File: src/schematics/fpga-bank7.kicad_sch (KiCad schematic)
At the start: 7 parts, among them U6 LFE5U-85F-*BG756*

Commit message: Add remaining component footprints (#79)
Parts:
- C78, C79, C80, C81, C82, C83: footprint (none) -> Capacitor_SMD:C_0402_1005Metric
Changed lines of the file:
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@@
 			)
 		)
-		(property "Footprint" ""
+		(property "Footprint" "Capacitor_SMD:C_0402_1005Metric"
 			(at 165.1 36.83 0)
 			(effects
@@
 			)
 		)
-		(property "Footprint" ""
+		(property "Footprint" "Capacitor_SMD:C_0402_1005Metric"
 			(at 153.67 36.83 0)
 			(effects
@@
 			)
 		)
-		(property "Footprint" ""
+		(property "Footprint" "Capacitor_SMD:C_0402_1005Metric"
 			(at 123.19 36.83 0)
 			(effects
@@
 			)
 		)
-		(property "Footprint" ""
+		(property "Footprint" "Capacitor_SMD:C_0402_1005Metric"
 			(at 133.35 36.83 0)
 			(effects
@@
 			)
 		)
-		(property "Footprint" ""
+		(property "Footprint" "Capacitor_SMD:C_0402_1005Metric"
 			(at 113.03 36.83 0)
 			(effects
@@
 			)
 		)
-		(property "Footprint" ""
+		(property "Footprint" "Capacitor_SMD:C_0402_1005Metric"
 			(at 143.51 36.83 0)
 			(effects

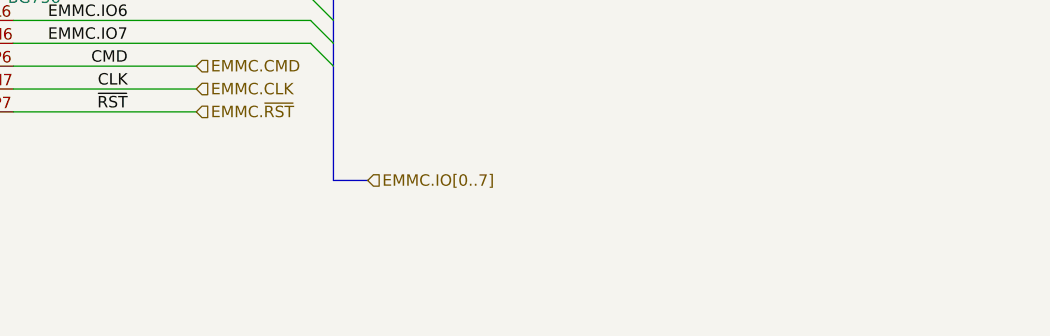
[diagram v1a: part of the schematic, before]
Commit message: Add notes on the schematic
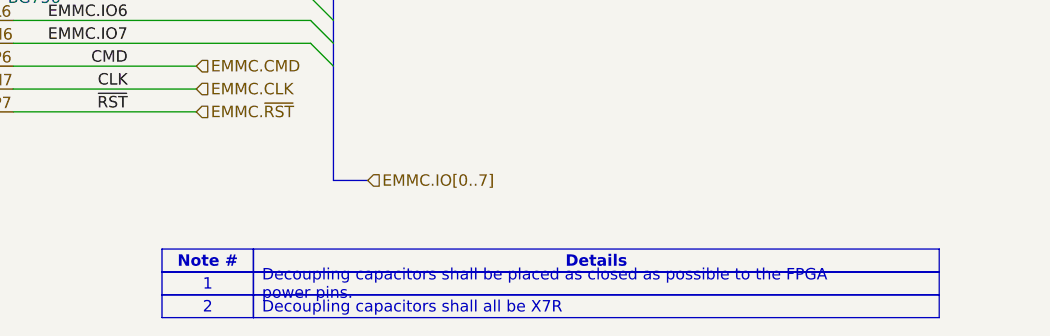
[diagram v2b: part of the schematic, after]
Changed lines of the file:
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@@
 		(comment 3 "${Part Number}")
+	)
+	(text_box "Decoupling capacitors shall all be X7R"
+		(exclude_from_sim no)
+		(at 203.2 167.64 0)
+		(size 76.2 2.54)
+		(margins 0.9525 0.9525 0.9525 0.9525)
+		(stroke
+			(width 0)
+			(type solid)
+			(color 0 0 0 1)
+		)
+		(fill
+			(type none)
+		)
+		(effects
+			(font
+				(face "Arial")
+				(size 1.27 1.27)
+				(color 0 0 0 1)
+			)
+			(justify left)
+		)
+	)
+	(text_box "Decoupling capacitors shall be placed as closed as possible to the FPGA power pins."
+		(exclude_from_sim no)
+		(at 203.2 165.1 0)
+		(size 76.2 2.54)
+		(margins 0.9525 0.9525 0.9525 0.9525)
+		(stroke
+			(width 0)
+			(type solid)
+			(color 0 0 0 1)
+		)
+		(fill
+			(type none)
+		)
+		(effects
+			(font
+				(face "Arial")
+				(size 1.27 1.27)
+				(color 0 0 0 1)
+			)
+			(justify left)
+		)
+	)
+	(text_box "2"
+		(exclude_from_sim no)
+		(at 193.04 167.64 0)
+		(size 10.16 2.54)
+		(margins 0.9525 0.9525 0.9525 0.9525)
+		(stroke
+			(width 0)
+			(type solid)
+			(color 0 0 0 1)
+		)
+		(fill
+			(type none)
+		)
+		(effects
+			(font
+				(face "Arial")
+				(size 1.27 1.27)
+				(color 0 0 0 1)
+			)
+		)
+	)
+	(text_box "Details"
+		(exclude_from_sim no)
+		(at 203.2 162.56 0)
+		(size 76.2 2.54)
+		(margins 0.9525 0.9525 0.9525 0.9525)
+		(stroke
+			(width 0)
+			(type solid)
+			(color 0 0 0 1)
+		)
+		(fill
+			(type none)
+		)
+		(effects
+			(font
+				(face "Arial")
+				(size 1.27 1.27)
+				(bold yes)
+				(color 0 0 0 1)
+			)
+		)
+	)
+	(text_box "Note #"
+		(exclude_from_sim no)
+		(at 193.04 162.56 0)
+		(size 10.16 2.54)
+		(margins 0.9525 0.9525 0.9525 0.9525)
+		(stroke
+			(width 0)
+			(type solid)
+			(color 0 0 0 1)
+		)
+		(fill
+			(type none)
+		)
+		(effects
+			(font
+				(face "Arial")
+				(size 1.27 1.27)
+				(bold yes)
+				(color 0 0 0 1)
+			)
+		)
+	)
+	(text_box "1"
+		(exclude_from_sim no)
+		(at 193.04 165.1 0)
+		(size 10.16 2.54)
+		(margins 0.9525 0.9525 0.9525 0.9525)
+		(stroke
+			(width 0)
+			(type solid)
+			(color 0 0 0 1)
+		)
+		(fill
+			(type none)
+		)
+		(effects
+			(font
+				(face "Arial")
+				(size 1.27 1.27)
+				(color 0 0 0 1)
+			)
+		)
 	)
 	(junction

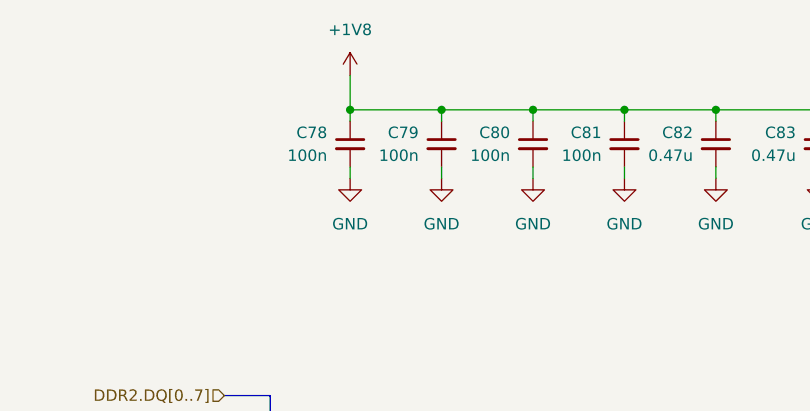
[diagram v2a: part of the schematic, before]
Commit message: Adds decoupling capacitors
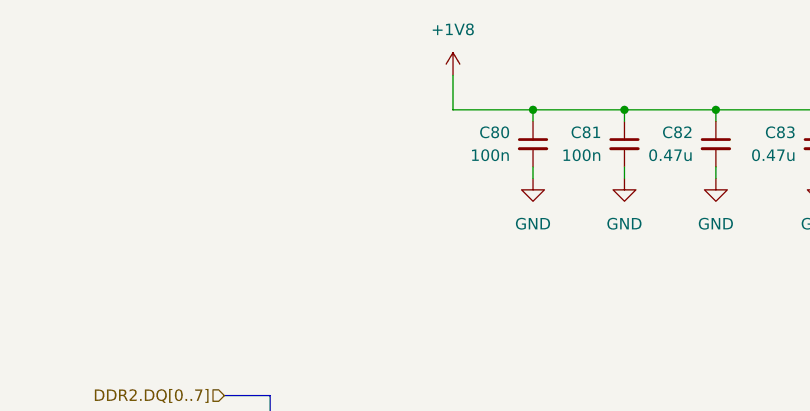
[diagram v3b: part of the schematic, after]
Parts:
- removed C78, C79: 100n, Capacitor_SMD:C_0402_1005Metric, symbol Device:C_Small
- C80, C81, C82, C83: footprint Capacitor_SMD:C_0402_1005Metric -> Capacitor_SMD:C_0201_0603Metric

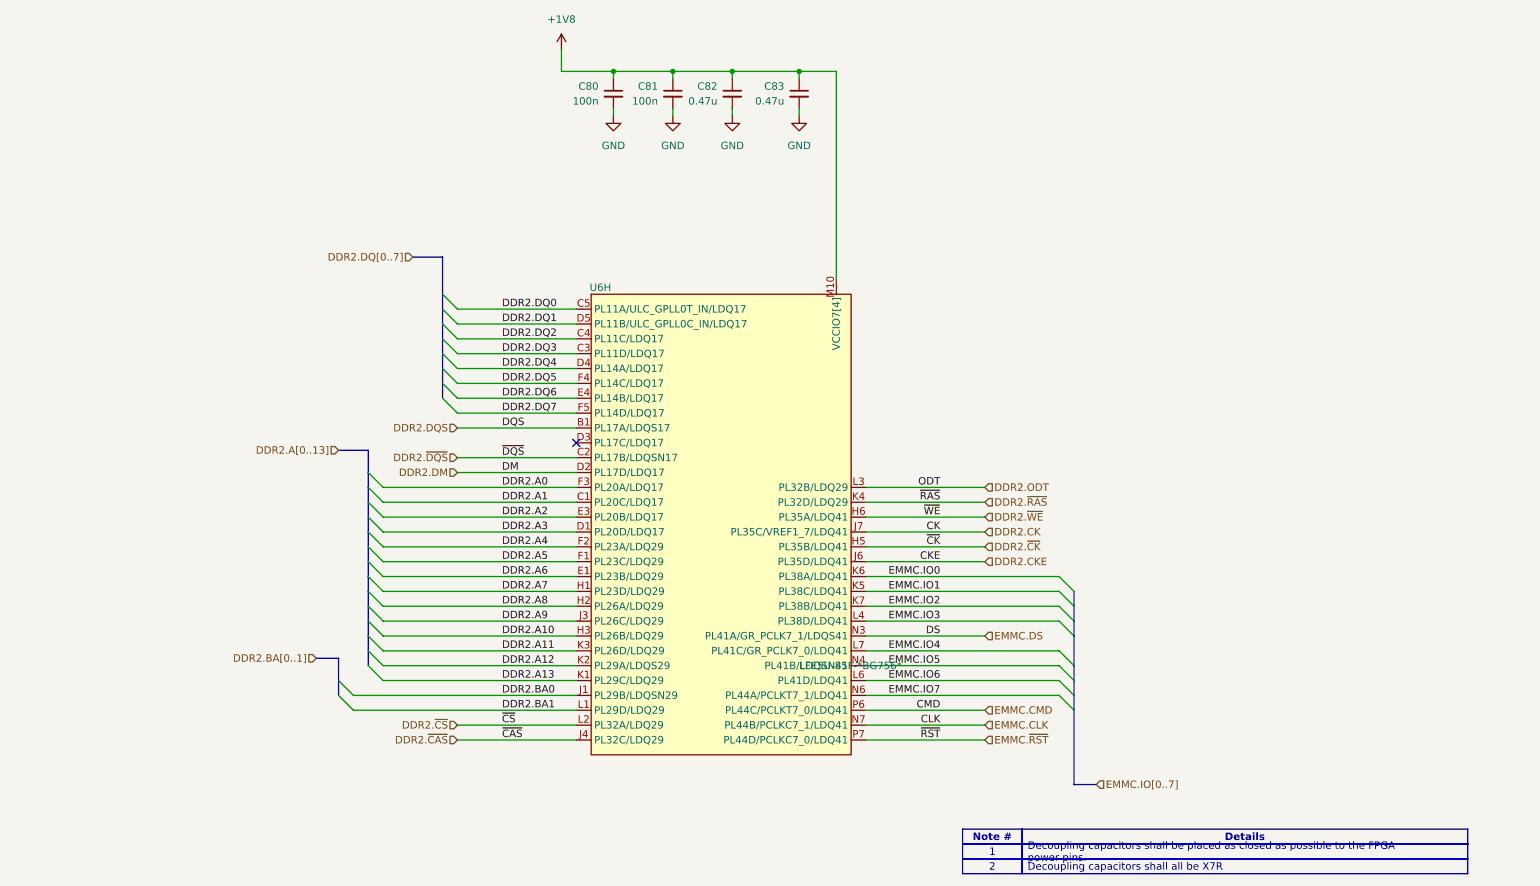
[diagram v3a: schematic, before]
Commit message: Move 1.8v converter to other side of the board
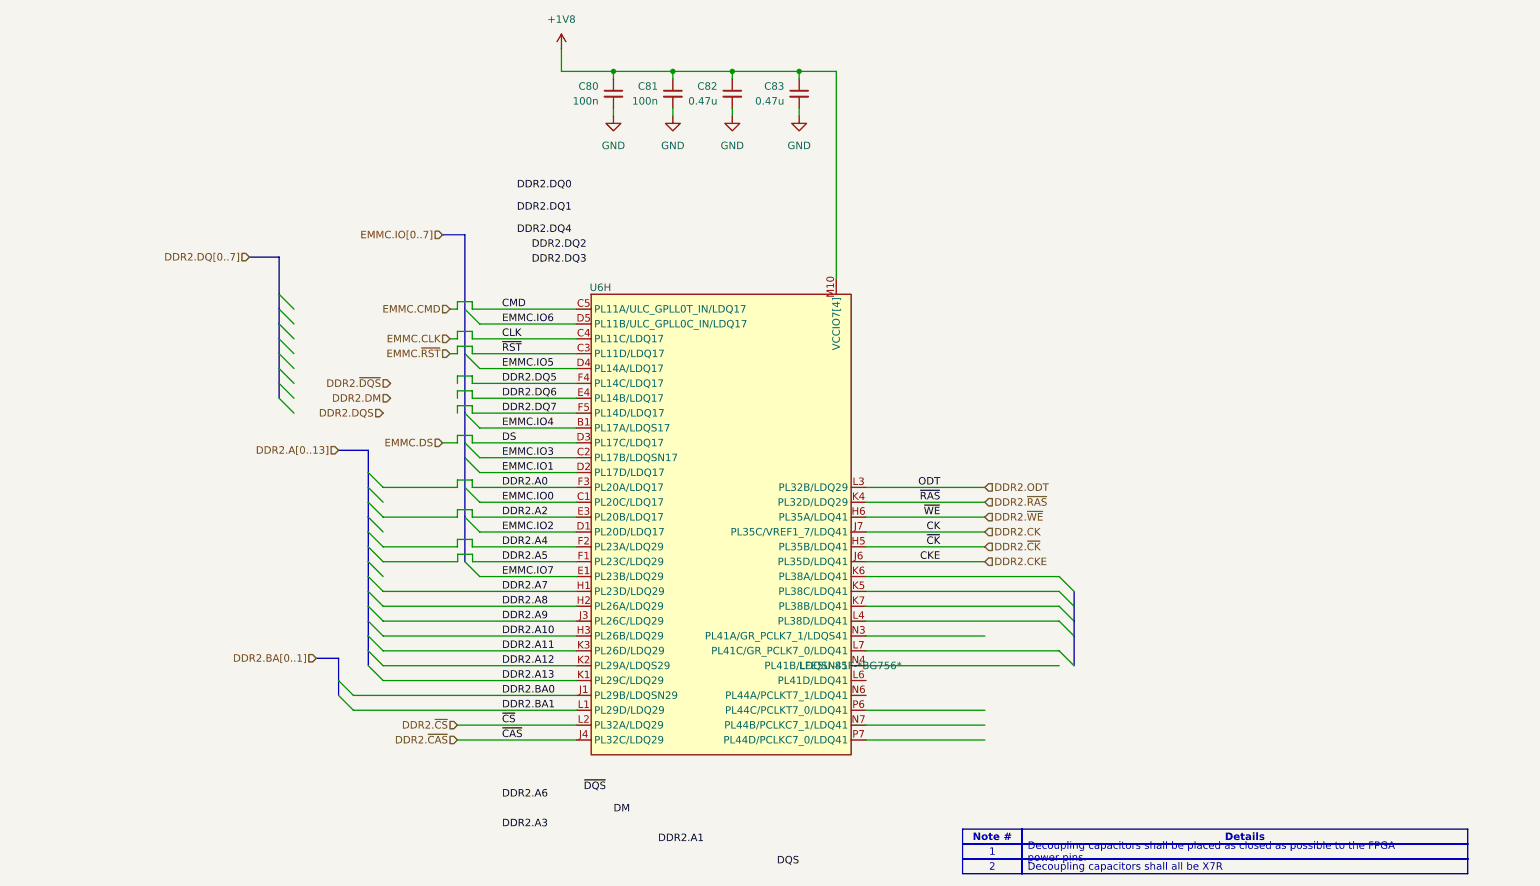
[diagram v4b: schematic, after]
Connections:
- net DDR2.A1: no longer U6.C1 (PL20C/LDQ17)
- net DDR2.A3: no longer U6.D1 (PL20D/LDQ17)
- net DDR2.A6: no longer U6.E1 (PL23B/LDQ29)
- net DDR2.DM: no longer U6.D2 (PL17D/LDQ17)
- net DDR2.DQ0: no longer U6.C5 (PL11A/ULC_GPLL0T_IN/LDQ17)
- net DDR2.DQ1: no longer U6.D5 (PL11B/ULC_GPLL0C_IN/LDQ17)
- net DDR2.DQ2: no longer U6.C4 (PL11C/LDQ17)
- net DDR2.DQ3: no longer U6.C3 (PL11D/LDQ17)
- net DDR2.DQ4: no longer U6.D4 (PL14A/LDQ17)
- net DDR2.DQS: no longer U6.B1 (PL17A/LDQS17)
- net DDR2.~{DQS}: no longer U6.C2 (PL17B/LDQSN17)
- net EMMC.CLK: now also U6.C4 (PL11C/LDQ17); no longer U6.N7 (PL44B/PCLKC7_1/LDQ41)
- net EMMC.CMD: now also U6.C5 (PL11A/ULC_GPLL0T_IN/LDQ17); no longer U6.P6 (PL44C/PCLKT7_0/LDQ41)
- net EMMC.DS: now also U6.D3 (PL17C/LDQ17); no longer U6.N3 (PL41A/GR_PCLK7_1/LDQS41)
- net EMMC.IO0: now also U6.C1 (PL20C/LDQ17); no longer U6.K6 (PL38A/LDQ41)
- net EMMC.IO1: now also U6.D2 (PL17D/LDQ17); no longer U6.K5 (PL38C/LDQ41)
- net EMMC.IO2: now also U6.D1 (PL20D/LDQ17); no longer U6.K7 (PL38B/LDQ41)
- net EMMC.IO3: now also U6.C2 (PL17B/LDQSN17); no longer U6.L4 (PL38D/LDQ41)
- net EMMC.IO4: now also U6.B1 (PL17A/LDQS17); no longer U6.L7 (PL41C/GR_PCLK7_0/LDQ41)
- net EMMC.IO5: now also U6.D4 (PL14A/LDQ17); no longer U6.N4 (PL41B/LDQSN41)
- net EMMC.IO6: now also U6.D5 (PL11B/ULC_GPLL0C_IN/LDQ17); no longer U6.L6 (PL41D/LDQ41)
- net EMMC.IO7: now also U6.E1 (PL23B/LDQ29); no longer U6.N6 (PL44A/PCLKT7_1/LDQ41)
- net EMMC.~{RST}: now also U6.C3 (PL11D/LDQ17); no longer U6.P7 (PL44D/PCLKC7_0/LDQ41)
- no-connect marks 1 -> 0

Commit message: Start routing DDR2 data lanes
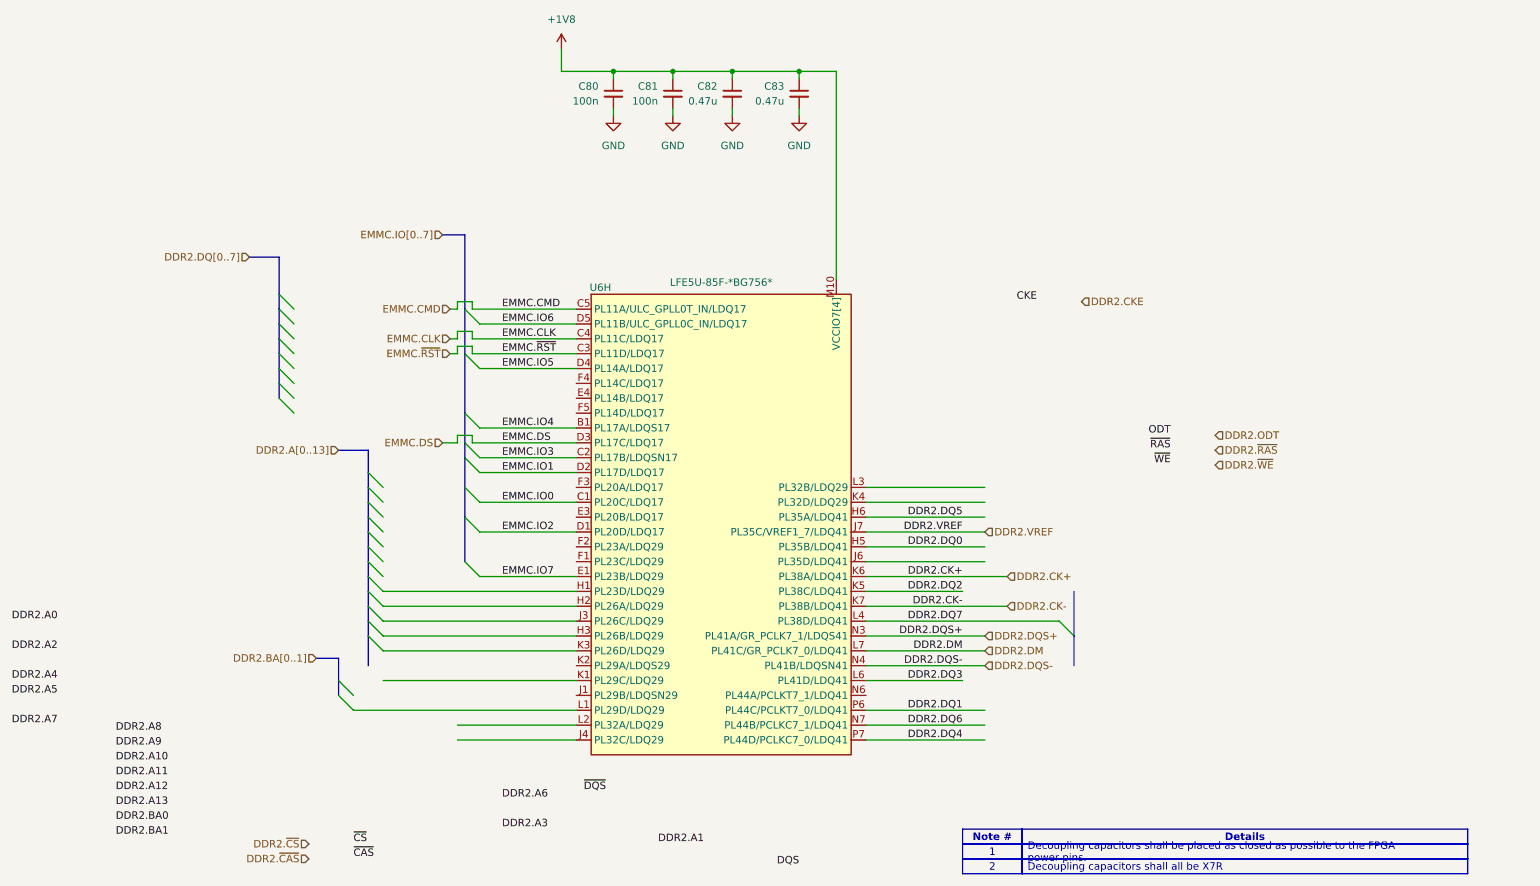
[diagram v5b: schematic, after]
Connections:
- net DDR2.~{CK} is gone; now on net DDR2.DQ0: U6.H5 (PL35B/LDQ41)
- net DDR2.A0: no longer U6.F3 (PL20A/LDQ17)
- net DDR2.A10: no longer U6.H3 (PL26B/LDQ29)
- net DDR2.A11: no longer U6.K3 (PL26D/LDQ29)
- net DDR2.A12: no longer U6.K2 (PL29A/LDQS29)
- net DDR2.A13: no longer U6.K1 (PL29C/LDQ29)
- net DDR2.A2: no longer U6.E3 (PL20B/LDQ17)
- net DDR2.A4: no longer U6.F2 (PL23A/LDQ29)
- net DDR2.A5: no longer U6.F1 (PL23C/LDQ29)
- net DDR2.A7: no longer U6.H1 (PL23D/LDQ29)
- net DDR2.A8: no longer U6.H2 (PL26A/LDQ29)
- net DDR2.A9: no longer U6.J3 (PL26C/LDQ29)
- net DDR2.BA0: no longer U6.J1 (PL29B/LDQSN29)
- net DDR2.BA1: no longer U6.L1 (PL29D/LDQ29)
- net DDR2.CKE: no longer U6.J6 (PL35D/LDQ41)
- net DDR2.DM: now also U6.L7 (PL41C/GR_PCLK7_0/LDQ41)
- net DDR2.DQ1: now also U6.P6 (PL44C/PCLKT7_0/LDQ41)
- net DDR2.DQ2: now also U6.K5 (PL38C/LDQ41)
- net DDR2.DQ3: now also U6.L6 (PL41D/LDQ41)
- net DDR2.DQ4: now also U6.P7 (PL44D/PCLKC7_0/LDQ41)
- net DDR2.DQ5: now also U6.H6 (PL35A/LDQ41); no longer U6.F4 (PL14C/LDQ17)
- net DDR2.DQ6: now also U6.N7 (PL44B/PCLKC7_1/LDQ41); no longer U6.E4 (PL14B/LDQ17)
- net DDR2.DQ7: now also U6.L4 (PL38D/LDQ41); no longer U6.F5 (PL14D/LDQ17)
- net DDR2.ODT: no longer U6.L3 (PL32B/LDQ29)
- net DDR2.~{CAS}: no longer U6.J4 (PL32C/LDQ29)
- net DDR2.~{CS}: no longer U6.L2 (PL32A/LDQ29)
- net DDR2.~{RAS}: no longer U6.K4 (PL32D/LDQ29)
- net DDR2.~{WE}: no longer U6.H6 (PL35A/LDQ41)
- net DDR2.CK+: now reaches U6.K6 (PL38A/LDQ41)
- net DDR2.CK-: now reaches U6.K7 (PL38B/LDQ41)
- net DDR2.DQS+: now reaches U6.N3 (PL41A/GR_PCLK7_1/LDQS41)
- net DDR2.DQS-: now reaches U6.N4 (PL41B/LDQSN41)
- net DDR2.CK renamed DDR2.VREF

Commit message: Route signals from DDR2 to FPGA bank
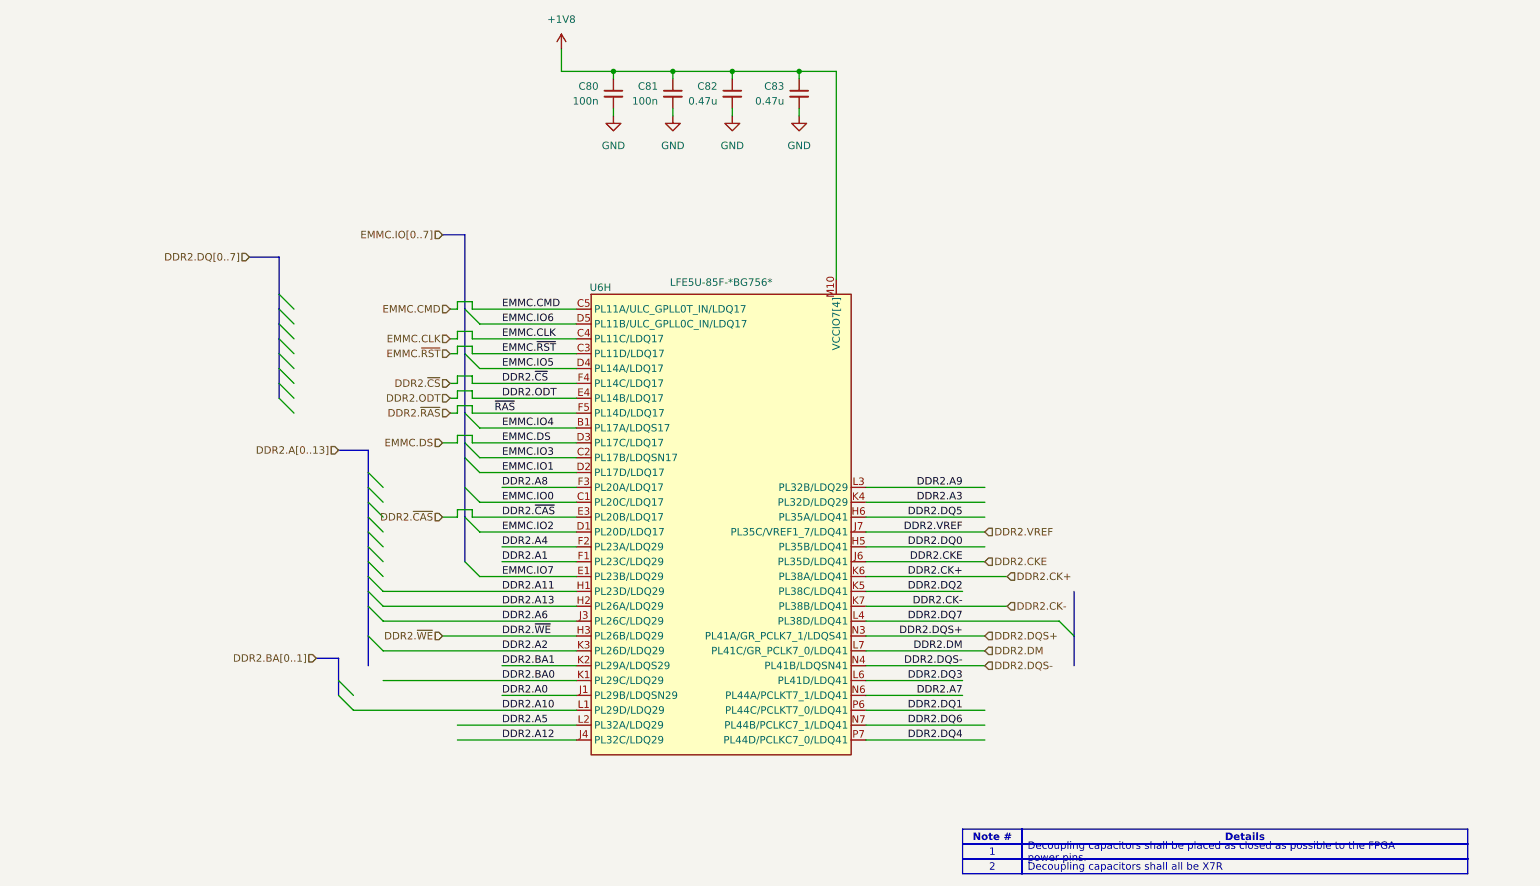
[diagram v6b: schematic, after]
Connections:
- net DDR2.A0: now also U6.J1 (PL29B/LDQSN29)
- net DDR2.A1: now also U6.F1 (PL23C/LDQ29)
- net DDR2.A10: now also U6.L1 (PL29D/LDQ29)
- net DDR2.A11: now also U6.H1 (PL23D/LDQ29)
- net DDR2.A12: now also U6.J4 (PL32C/LDQ29)
- net DDR2.A13: now also U6.H2 (PL26A/LDQ29)
- net DDR2.A2: now also U6.K3 (PL26D/LDQ29)
- net DDR2.A3: now also U6.K4 (PL32D/LDQ29)
- net DDR2.A4: now also U6.F2 (PL23A/LDQ29)
- net DDR2.A5: now also U6.L2 (PL32A/LDQ29)
- net DDR2.A6: now also U6.J3 (PL26C/LDQ29)
- net DDR2.A7: now also U6.N6 (PL44A/PCLKT7_1/LDQ41)
- net DDR2.A8: now also U6.F3 (PL20A/LDQ17)
- net DDR2.A9: now also U6.L3 (PL32B/LDQ29)
- net DDR2.BA0: now also U6.K1 (PL29C/LDQ29)
- net DDR2.BA1: now also U6.K2 (PL29A/LDQS29)
- net DDR2.CKE: now also U6.J6 (PL35D/LDQ41)
- net DDR2.ODT: now also U6.E4 (PL14B/LDQ17)
- net DDR2.~{CAS}: now also U6.E3 (PL20B/LDQ17)
- net DDR2.~{CS}: now also U6.F4 (PL14C/LDQ17)
- net DDR2.~{RAS}: now also U6.F5 (PL14D/LDQ17)
- net DDR2.~{WE}: now also U6.H3 (PL26B/LDQ29)
